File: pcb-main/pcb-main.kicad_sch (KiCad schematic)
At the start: 37 parts, among them J1 AVR-ISP-6, J2 Conn_02x06_Counter_Clockwise, M1 Stepper_Motor, SW1 SW_MEC_5E, SW2 SW_MEC_5E, U1 ATmega328P-AU, U2 HT1621B-LQFP-A, U3 VIM878, U4 PCF8563T, Y1 16MHz, Y2 32kHz

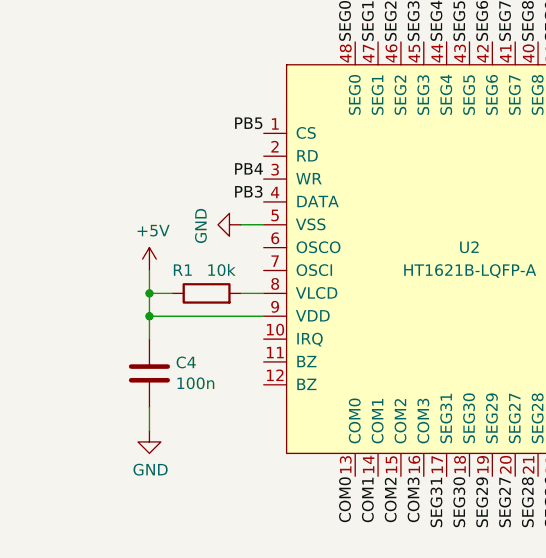
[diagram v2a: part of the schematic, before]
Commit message: resolves #13: lcd brightness pot
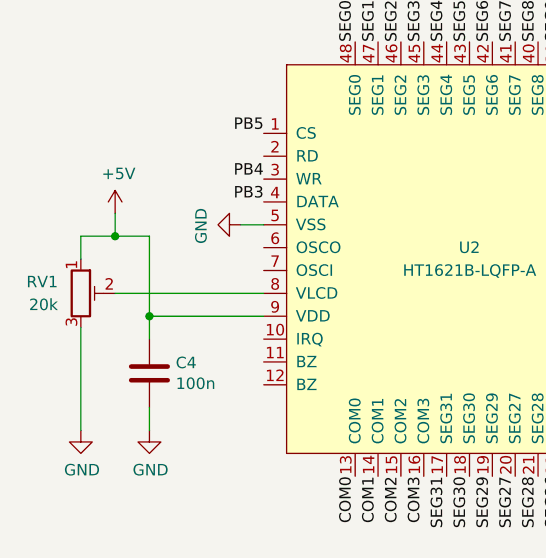
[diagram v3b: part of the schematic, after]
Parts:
- removed R1: 10k, Resistor_SMD:R_1206_3216Metric_Pad1.30x1.75mm_HandSolder, symbol Device:R
- added RV1: 20k, Potentiometer_SMD:Potentiometer_Bourns_TC33X_Vertical, symbol Device:R_Potentiometer_Trim
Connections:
- net +5V: now also RV1.1
- net GND: now also RV1.3
- net at U2.8 (VLCD): now also RV1.2
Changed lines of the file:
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@@
   (junction (at 262.89 24.13) (diameter 0) (color 0 0 0 0)
   )
+  (junction (at 34.29 163.83) (diameter 0) (color 0 0 0 0)
+  )
   (junction (at 273.05 36.83) (diameter 0) (color 0 0 0 0)
   )
   (junction (at 227.33 63.5) (diameter 0) (color 0 0 0 0)
   )
+  (junction (at 30.48 154.94) (diameter 0) (color 0 0 0 0)
+  )
   (junction (at 186.69 36.83) (diameter 0) (color 0 0 0 0)
   )
-  (junction (at 34.29 161.29) (diameter 0) (color 0 0 0 0)
-  )
   (junction (at 105.41 90.17) (diameter 0) (color 0 0 0 0)
   )
   (junction (at 118.11 36.83) (diameter 0) (color 0 0 0 0)
   )
-  (junction (at 34.29 163.83) (diameter 0) (color 0 0 0 0)
-  )
   (junction (at 118.11 90.17) (diameter 0) (color 0 0 0 0)
   )
@@
     (stroke (width 0) (type default) (color 0 0 0 0))
   )
-  (wire (pts (xy 36.83 161.29) (xy 34.29 161.29))
-    (stroke (width 0) (type default) (color 0 0 0 0))
-  )
   (wire (pts (xy 54.61 22.86) (xy 54.61 25.4))
     (stroke (width 0) (type default) (color 0 0 0 0))
   )
+  (wire (pts (xy 34.29 163.83) (xy 34.29 154.94))
+    (stroke (width 0) (type default) (color 0 0 0 0))
+  )
   (wire (pts (xy 186.69 39.37) (xy 189.23 39.37))
     (stroke (width 0) (type default) (color 0 0 0 0))
@@
     (stroke (width 0) (type default) (color 0 0 0 0))
   )
-  (wire (pts (xy 34.29 161.29) (xy 34.29 163.83))
+  (wire (pts (xy 26.67 154.94) (xy 26.67 157.48))
     (stroke (width 0) (type default) (color 0 0 0 0))
   )
@@
     (stroke (width 0) (type default) (color 0 0 0 0))
   )
-  (wire (pts (xy 46.99 161.29) (xy 44.45 161.29))
-    (stroke (width 0) (type default) (color 0 0 0 0))
-  )
-  (wire (pts (xy 34.29 161.29) (xy 34.29 158.75))
-    (stroke (width 0) (type default) (color 0 0 0 0))
-  )
   (wire (pts (xy 229.87 146.05) (xy 229.87 148.59))
     (stroke (width 0) (type default) (color 0 0 0 0))
@@
     (stroke (width 0) (type default) (color 0 0 0 0))
   )
+  (wire (pts (xy 34.29 154.94) (xy 30.48 154.94))
+    (stroke (width 0) (type default) (color 0 0 0 0))
+  )
   (wire (pts (xy 195.58 135.89) (xy 207.01 135.89))
     (stroke (width 0) (type default) (color 0 0 0 0))
@@
     (stroke (width 0) (type default) (color 0 0 0 0))
   )
+  (wire (pts (xy 30.48 152.4) (xy 30.48 154.94))
+    (stroke (width 0) (type default) (color 0 0 0 0))
+  )
+  (wire (pts (xy 26.67 165.1) (xy 26.67 176.53))
+    (stroke (width 0) (type default) (color 0 0 0 0))
+  )
   (wire (pts (xy 201.93 39.37) (xy 201.93 36.83))
     (stroke (width 0) (type default) (color 0 0 0 0))
@@
     (stroke (width 0) (type default) (color 0 0 0 0))
   )
+  (wire (pts (xy 30.48 154.94) (xy 26.67 154.94))
+    (stroke (width 0) (type default) (color 0 0 0 0))
+  )
   (wire (pts (xy 184.15 36.83) (xy 186.69 36.83))
     (stroke (width 0) (type default) (color 0 0 0 0))
@@
   )
   (wire (pts (xy 102.87 36.83) (xy 105.41 36.83))
+    (stroke (width 0) (type default) (color 0 0 0 0))
+  )
+  (wire (pts (xy 30.48 161.29) (xy 46.99 161.29))
     (stroke (width 0) (type default) (color 0 0 0 0))
   )
@@
     (pin "1")
   )
-  (symbol (lib_id "power:+5V") (at 34.29 158.75 0) (unit 1)
-    (in_bom yes) (on_board yes)
-    (property "Reference" "#PWR0109" (id 0) (at 34.29 162.56 0)
-      (effects (font (size 1.27 1.27)) hide)
-    )
-    (property "Value" "+5V" (id 1) (at 34.671 154.3558 0))
-    (property "Footprint" "" (id 2) (at 34.29 158.75 0)
-      (effects (font (size 1.27 1.27)) hide)
-    )
-    (property "Datasheet" "" (id 3) (at 34.29 158.75 0)
+  (symbol (lib_id "power:+5V") (at 30.48 152.4 0) (unit 1)
+    (in_bom yes) (on_board yes)
+    (property "Reference" "#PWR0109" (id 0) (at 30.48 156.21 0)
+      (effects (font (size 1.27 1.27)) hide)
+    )
+    (property "Value" "+5V" (id 1) (at 30.861 148.0058 0))
+    (property "Footprint" "" (id 2) (at 30.48 152.4 0)
+      (effects (font (size 1.27 1.27)) hide)
+    )
+    (property "Datasheet" "" (id 3) (at 30.48 152.4 0)
       (effects (font (size 1.27 1.27)) hide)
     )
@@
     (pin "2")
   )
-  (symbol (lib_id "power:GND") (at 34.29 176.53 0) (unit 1)
-    (in_bom yes) (on_board yes)
-    (property "Reference" "#PWR0107" (id 0) (at 34.29 182.88 0)
-      (effects (font (size 1.27 1.27)) hide)
-    )
-    (property "Value" "GND" (id 1) (at 34.417 180.9242 0))
-    (property "Footprint" "" (id 2) (at 34.29 176.53 0)
-      (effects (font (size 1.27 1.27)) hide)
-    )
-    (property "Datasheet" "" (id 3) (at 34.29 176.53 0)
+  (symbol (lib_id "power:GND") (at 26.67 176.53 0) (unit 1)
+    (in_bom yes) (on_board yes)
+    (property "Reference" "#PWR0107" (id 0) (at 26.67 182.88 0)
+      (effects (font (size 1.27 1.27)) hide)
+    )
+    (property "Value" "GND" (id 1) (at 26.797 180.9242 0))
+    (property "Footprint" "" (id 2) (at 26.67 176.53 0)
+      (effects (font (size 1.27 1.27)) hide)
+    )
+    (property "Datasheet" "" (id 3) (at 26.67 176.53 0)
       (effects (font (size 1.27 1.27)) hide)
     )
@@
     )
     (pin "1")
-  )
-  (symbol (lib_id "Device:R") (at 40.64 161.29 90) (unit 1)
-    (in_bom yes) (on_board yes)
-    (property "Reference" "R1" (id 0) (at 36.83 158.75 90)
-      (effects (font (size 1.27 1.27)) (justify right))
-    )
-    (property "Value" "10k" (id 1) (at 40.64 158.75 90)
-      (effects (font (size 1.27 1.27)) (justify right))
-    )
-    (property "Footprint" "Resistor_SMD:R_1206_3216Metric_Pad1.30x1.75mm_HandSolder" (id 2) (at 40.64 163.068 90)
-      (effects (font (size 1.27 1.27)) hide)
-    )
-    (property "Datasheet" "~" (id 3) (at 40.64 161.29 0)
-      (effects (font (size 1.27 1.27)) hide)
-    )
-    (pin "1")
-    (pin "2")
   )
   (symbol (lib_id "Timer_RTC:PCF8563T") (at 217.17 140.97 0) (unit 1)
@@
     (pin "1")
   )
+  (symbol (lib_id "Device:R_Potentiometer_Trim") (at 26.67 161.29 0) (unit 1)
+    (in_bom yes) (on_board yes) (fields_autoplaced)
+    (property "Reference" "RV1" (id 0) (at 24.13 160.0199 0)
+      (effects (font (size 1.27 1.27)) (justify right))
+    )
+    (property "Value" "20k" (id 1) (at 24.13 162.5599 0)
+      (effects (font (size 1.27 1.27)) (justify right))
+    )
+    (property "Footprint" "Potentiometer_SMD:Potentiometer_Bourns_TC33X_Vertical" (id 2) (at 26.67 161.29 0)
+      (effects (font (size 1.27 1.27)) hide)
+    )
+    (property "Datasheet" "~" (id 3) (at 26.67 161.29 0)
+      (effects (font (size 1.27 1.27)) hide)
+    )
+    (pin "1")
+    (pin "2")
+    (pin "3")
+  )
+  (symbol (lib_id "power:GND") (at 34.29 176.53 0) (unit 1)
+    (in_bom yes) (on_board yes)
+    (property "Reference" "#PWR0135" (id 0) (at 34.29 182.88 0)
+      (effects (font (size 1.27 1.27)) hide)
+    )
+    (property "Value" "GND" (id 1) (at 34.417 180.9242 0))
+    (property "Footprint" "" (id 2) (at 34.29 176.53 0)
+      (effects (font (size 1.27 1.27)) hide)
+    )
+    (property "Datasheet" "" (id 3) (at 34.29 176.53 0)
+      (effects (font (size 1.27 1.27)) hide)
+    )
+    (pin "1")
+  )
   (symbol (lib_id "power:GND") (at 201.93 41.91 0) (unit 1)
     (in_bom yes) (on_board yes)
@@
       (reference "#PWR0134") (unit 1) (value "GND") (footprint "")
     )
+    (path "/9fd85478-c8a4-4520-a7c7-b743dd04a466"
+      (reference "#PWR0135") (unit 1) (value "GND") (footprint "")
+    )
     (path "/00000000-0000-0000-0000-000061a65214"
       (reference "BT1") (unit 1) (value "Battery_Cell") (footprint "footprints:CR1220")
@@
       (reference "M1") (unit 1) (value "Stepper_Motor") (footprint "footprints:Stepper Motor")
     )
-    (path "/00000000-0000-0000-0000-0000619dcc9f"
-      (reference "R1") (unit 1) (value "10k") (footprint "Resistor_SMD:R_1206_3216Metric_Pad1.30x1.75mm_HandSolder")
-    )
     (path "/00000000-0000-0000-0000-000061a7ca87"
       (reference "R2") (unit 1) (value "10k") (footprint "Resistor_SMD:R_1206_3216Metric_Pad1.30x1.75mm_HandSolder")
@@
       (reference "R7") (unit 1) (value "10k") (footprint "Resistor_SMD:R_1206_3216Metric_Pad1.30x1.75mm_HandSolder")
     )
+    (path "/56197513-6506-4a24-beee-dd8ea3402d50"
+      (reference "RV1") (unit 1) (value "20k") (footprint "Potentiometer_SMD:Potentiometer_Bourns_TC33X_Vertical")
+    )
     (path "/00000000-0000-0000-0000-000061bb50e2"

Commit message: resolves #39: smd crystals
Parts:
- Y1: footprint Crystal:Crystal_HC49-4H_Vertical -> Crystal:Crystal_SMD_3225-4Pin_3.2x2.5mm
- Y2: footprint Crystal:Crystal_C26-LF_D2.1mm_L6.5mm_Horizontal -> Crystal:Crystal_SMD_3215-2Pin_3.2x1.5mm
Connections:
- net GND: now also C2.1; no longer C2.2
- net XTAL1: now also C3.1, Y1.2; no longer C2.1, Y1.1
- net XTAL2: now also C2.2, Y1.1; no longer C3.1, Y1.2
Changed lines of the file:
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@@
     (effects (font (size 1.27 1.27)) (justify right bottom))
   )
-  (label "XTAL2" (at 118.11 87.63 0)
-    (effects (font (size 1.27 1.27)) (justify left bottom))
+  (label "XTAL2" (at 105.41 87.63 180)
+    (effects (font (size 1.27 1.27)) (justify right bottom))
   )
   (label "SEG25" (at 82.55 181.61 270)
@@
     (effects (font (size 1.27 1.27)) (justify left bottom))
   )
-  (label "XTAL1" (at 105.41 87.63 180)
-    (effects (font (size 1.27 1.27)) (justify right bottom))
+  (label "XTAL1" (at 118.11 87.63 0)
+    (effects (font (size 1.27 1.27)) (justify left bottom))
   )
   (label "SEG15" (at 142.24 175.26 0)
@@
     (property "Reference" "Y1" (id 0) (at 111.76 83.3628 0))
     (property "Value" "16MHz" (id 1) (at 111.76 85.6742 0))
-    (property "Footprint" "Crystal:Crystal_HC49-4H_Vertical" (id 2) (at 111.76 90.17 0)
-      (effects (font (size 1.27 1.27)) hide)
-    )
-    (property "Datasheet" "~" (id 3) (at 111.76 90.17 0)
-      (effects (font (size 1.27 1.27)) hide)
-    )
-    (pin "1")
-    (pin "2")
-  )
-  (symbol (lib_id "Device:C") (at 105.41 96.52 0) (unit 1)
-    (in_bom yes) (on_board yes)
-    (property "Reference" "C2" (id 0) (at 108.331 95.3516 0)
-      (effects (font (size 1.27 1.27)) (justify left))
-    )
-    (property "Value" "22p" (id 1) (at 108.331 97.663 0)
-      (effects (font (size 1.27 1.27)) (justify left))
-    )
-    (property "Footprint" "Capacitor_SMD:C_1206_3216Metric_Pad1.33x1.80mm_HandSolder" (id 2) (at 106.3752 100.33 0)
+    (property "Footprint" "Crystal:Crystal_SMD_3225-4Pin_3.2x2.5mm" (id 2) (at 111.76 90.17 0)
+      (effects (font (size 1.27 1.27)) hide)
+    )
+    (property "Datasheet" "https://datasheet.lcsc.com/lcsc/2103291133_Yangxing-Tech-X322516MLB4SI_C13738.pdf" (id 3) (at 111.76 90.17 0)
+      (effects (font (size 1.27 1.27)) hide)
+    )
+    (pin "1")
+    (pin "2")
+  )
+  (symbol (lib_name "C_1") (lib_id "Device:C") (at 105.41 96.52 180) (unit 1)
+    (in_bom yes) (on_board yes)
+    (property "Reference" "C2" (id 0) (at 102.489 97.6884 0)
+      (effects (font (size 1.27 1.27)) (justify left))
+    )
+    (property "Value" "22p" (id 1) (at 102.489 95.377 0)
+      (effects (font (size 1.27 1.27)) (justify left))
+    )
+    (property "Footprint" "Capacitor_SMD:C_1206_3216Metric_Pad1.33x1.80mm_HandSolder" (id 2) (at 104.4448 92.71 0)
       (effects (font (size 1.27 1.27)) hide)
     )
@@
       (effects (font (size 1.27 1.27)) (justify left))
     )
-    (property "Footprint" "Crystal:Crystal_C26-LF_D2.1mm_L6.5mm_Horizontal" (id 2) (at 195.58 140.97 0)
-      (effects (font (size 1.27 1.27)) hide)
-    )
-    (property "Datasheet" "~" (id 3) (at 195.58 140.97 0)
+    (property "Footprint" "Crystal:Crystal_SMD_3215-2Pin_3.2x1.5mm" (id 2) (at 195.58 140.97 0)
+      (effects (font (size 1.27 1.27)) hide)
+    )
+    (property "Datasheet" "https://datasheet.lcsc.com/lcsc/1810171817_Seiko-Epson-Q13FC1350000400_C32346.pdf" (id 3) (at 195.58 140.97 0)
       (effects (font (size 1.27 1.27)) hide)
     )
@@
     )
     (path "/00000000-0000-0000-0000-00006149bb4a"
-      (reference "Y1") (unit 1) (value "16MHz") (footprint "Crystal:Crystal_HC49-4H_Vertical")
+      (reference "Y1") (unit 1) (value "16MHz") (footprint "Crystal:Crystal_SMD_3225-4Pin_3.2x2.5mm")
     )
     (path "/00000000-0000-0000-0000-000061a72108"
-      (reference "Y2") (unit 1) (value "32kHz") (footprint "Crystal:Crystal_C26-LF_D2.1mm_L6.5mm_Horizontal")
-    )
-  )
+      (reference "Y2") (unit 1) (value "32kHz") (footprint "Crystal:Crystal_SMD_3215-2Pin_3.2x1.5mm")
+    )
+  )
